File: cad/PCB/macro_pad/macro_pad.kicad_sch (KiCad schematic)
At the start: 35 parts, among them SW1 SW_Push, SW10 SW_Push, SW11 SW_Push, SW12 SW_Push, SW13 SW_Push, SW14 SW_Push, SW15 SW_Push, SW16 SW_Push, SW17 RotaryEncoder_Switch, SW2 SW_Push, SW3 SW_Push, SW4 SW_Push, SW5 SW_Push, SW6 SW_Push, SW7 SW_Push, SW8 SW_Push, SW9 SW_Push, U1 XIAO-SAMD21-DIP

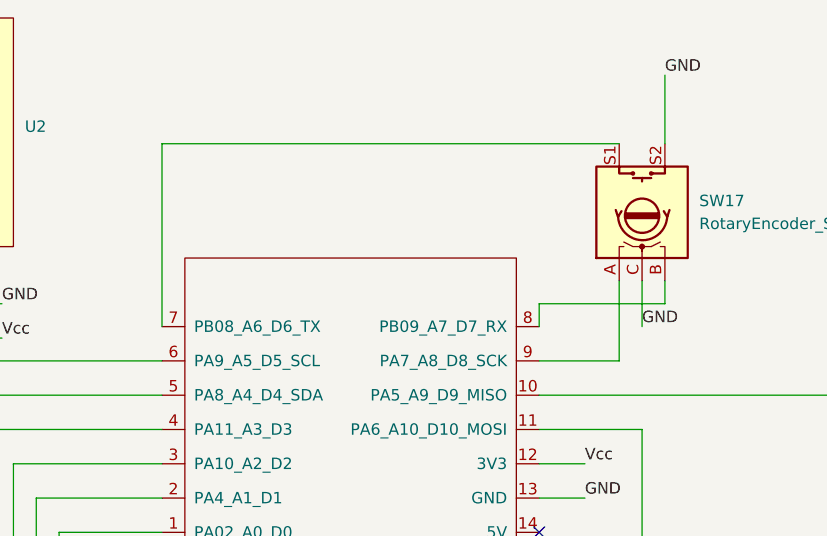
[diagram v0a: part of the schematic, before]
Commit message: moved encoder and mcu
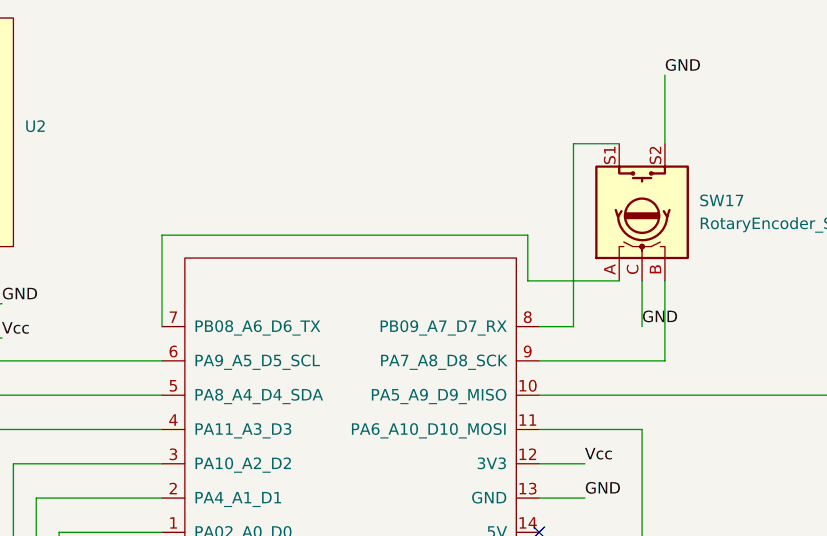
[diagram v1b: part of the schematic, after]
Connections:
- net at U1.7 (PB08_A6_D6_TX): now also SW17.A; no longer SW17.S1
- net at U1.8 (PB09_A7_D7_RX): now also SW17.S1; no longer SW17.B
- net at U1.9 (PA7_A8_D8_SCK): now also SW17.B; no longer SW17.A
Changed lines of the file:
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@@
-	(wire
-		(pts
-			(xy 99.06 43.18) (xy 99.06 52.07)
-		)
-		(stroke
-			(width 0)
-			(type default)
-		)
-	)
 	(wire
 		(pts
@@
 	(wire
 		(pts
-			(xy 90.17 45.72) (xy 90.17 48.26)
-		)
-		(stroke
-			(width 0)
-			(type default)
-		)
-	)
-	(wire
-		(pts
 			(xy 133.35 55.88) (xy 133.35 73.66)
 		)
@@
 	(wire
 		(pts
+			(xy 88.9 38.1) (xy 48.26 38.1)
+		)
+		(stroke
+			(width 0)
+			(type default)
+		)
+	)
+	(wire
+		(pts
 			(xy 30.48 45.72) (xy 27.94 45.72)
 		)
@@
 	(wire
 		(pts
+			(xy 48.26 38.1) (xy 48.26 48.26)
+		)
+		(stroke
+			(width 0)
+			(type default)
+		)
+	)
+	(wire
+		(pts
 			(xy 91.44 119.38) (xy 106.68 119.38)
 		)
@@
 	(wire
 		(pts
+			(xy 88.9 43.18) (xy 88.9 38.1)
+		)
+		(stroke
+			(width 0)
+			(type default)
+		)
+	)
+	(wire
+		(pts
+			(xy 93.98 48.26) (xy 90.17 48.26)
+		)
+		(stroke
+			(width 0)
+			(type default)
+		)
+	)
+	(wire
+		(pts
 			(xy 123.19 132.08) (xy 138.43 132.08)
 		)
@@
 	(wire
 		(pts
+			(xy 99.06 43.18) (xy 88.9 43.18)
+		)
+		(stroke
+			(width 0)
+			(type default)
+		)
+	)
+	(wire
+		(pts
 			(xy 148.59 127) (xy 148.59 139.7)
 		)
@@
 	(wire
 		(pts
-			(xy 104.14 45.72) (xy 90.17 45.72)
-		)
-		(stroke
-			(width 0)
-			(type default)
-		)
-	)
-	(wire
-		(pts
 			(xy 116.84 114.3) (xy 116.84 127)
 		)
@@
 	(wire
 		(pts
+			(xy 99.06 27.94) (xy 93.98 27.94)
+		)
+		(stroke
+			(width 0)
+			(type default)
+		)
+	)
+	(wire
+		(pts
 			(xy 106.68 93.98) (xy 123.19 93.98)
 		)
@@
 	(wire
 		(pts
-			(xy 48.26 27.94) (xy 48.26 48.26)
-		)
-		(stroke
-			(width 0)
-			(type default)
-		)
-	)
-	(wire
-		(pts
 			(xy 34.29 119.38) (xy 34.29 67.31)
 		)
@@
 	(wire
 		(pts
+			(xy 104.14 52.07) (xy 90.17 52.07)
+		)
+		(stroke
+			(width 0)
+			(type default)
+		)
+	)
+	(wire
+		(pts
 			(xy 106.68 119.38) (xy 123.19 119.38)
 		)
@@
 	(wire
 		(pts
+			(xy 104.14 43.18) (xy 104.14 52.07)
+		)
+		(stroke
+			(width 0)
+			(type default)
+		)
+	)
+	(wire
+		(pts
 			(xy 36.83 132.08) (xy 36.83 71.12)
 		)
@@
 	(wire
 		(pts
-			(xy 99.06 27.94) (xy 48.26 27.94)
-		)
-		(stroke
-			(width 0)
-			(type default)
-		)
-	)
-	(wire
-		(pts
 			(xy 101.6 59.69) (xy 101.6 73.66)
 		)
@@
 	(wire
 		(pts
-			(xy 104.14 43.18) (xy 104.14 45.72)
-		)
-		(stroke
-			(width 0)
-			(type default)
-		)
-	)
-	(wire
-		(pts
 			(xy 101.6 127) (xy 101.6 139.7)
 		)
@@
 	(wire
 		(pts
+			(xy 93.98 27.94) (xy 93.98 48.26)
+		)
+		(stroke
+			(width 0)
+			(type default)
+		)
+	)
+	(wire
+		(pts
 			(xy 25.4 41.91) (xy 25.4 49.53)
 		)
 		(stroke
-			(width 0)
-			(type default)
-		)
-	)
-	(wire
-		(pts
-			(xy 99.06 52.07) (xy 90.17 52.07)
-		)
-		(stroke
